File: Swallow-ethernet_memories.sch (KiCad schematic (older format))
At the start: 19 parts, among them P10 A0_Sel, P6 I2C, U10 DRAM-2MX16X4, U8 INA219, U9 S25FL064K

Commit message: Created pinout for SDRAM + ethernet I/O board. Pushed pinout to schematic.
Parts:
- removed C5: 220nF, SM0603, symbol C
- removed P10: A0_Sel, symbol CONN_3
- removed P6: I2C, PIN_ARRAY_4x1, symbol CONN_4
- removed R13, R15: 10R, SM0402, symbol R
- removed R14: 0R1, SM0805, symbol R
- removed R16, R17: 3k3, SM0402, symbol R
- removed U8: INA219, SOT23-8, symbol INA219
- removed W13: A11, TestPad-1mm, symbol TESTPOINT
- removed W14: A12, TestPad-1mm, symbol TESTPOINT
- removed W19: P1G, symbol TESTPOINT
- removed W20: P1F, symbol TESTPOINT
- removed W21: P1K, symbol TESTPOINT
- added P?: Ethernet_Slice, symbol CONN_PCIE-36
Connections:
- net labels added: A1, A2, A3, A4, A5, A6, A7, A8, A9, RESET_N, XLC0i, XLC0o, XLC1i, XLC1o, XLC2i, XLC2o, XLC3i, XLC3o, XLC4i, XLC4o
- net labels removed: P1F, P1G, P1K, SCK, SDA, XLB0i, XLB0o, XLB1i, XLB1o, XLB2i, XLB2o, XLB3i, XLB3o, XLB4i, XLB4o
- wire segments 228 -> 214
- no-connect marks 0 -> 14
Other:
- note added: "B17 is unused INT_N\nB18 in unused RXER"
- note removed: "A12 or D_CLK_EN"
- note removed: "C+D : DRAM Data x16"
- note removed: "DRAM : CLK, CLKEN\nI2C : Clk, Data0, Data1?"
- note removed: "DRAM Address A"
- note removed: "DRAM Current Sensor"
- note removed: "DRAM\nDecoupling"
- note removed: "I2C"
- moved on the sheet: C6, C7

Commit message: Completed schematic.
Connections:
- net labels removed: P32A0
- wire segments 214 -> 209
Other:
- note removed: "Swapped RAS & CAS for library compatibility"
- note removed: "These two pins can be re-used for DRAM clock generation if SPI_SS is set to high(disabled).\n\nOr can they? Since their types are declared "on stdcore[]""
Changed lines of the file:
@@
-EESchema Schematic File Version 2  date 30/09/2012 20:10:30
+EESchema Schematic File Version 2  date 30/09/2012 22:11:50
 LIBS:power
 LIBS:device
@@
 	6300 2400 7250 2400
 Wire Wire Line
-	6300 700  6650 700
-Wire Wire Line
-	6650 700  6650 600
-Wire Wire Line
-	6650 600  9100 600
-Wire Wire Line
 	6300 900  6800 900
 Wire Wire Line
@@
 Wire Wire Line
 	9250 1400 8450 1400
-Wire Wire Line
-	9400 700  9100 700
-Wire Wire Line
-	9100 700  9100 600
 Wire Wire Line
 	10650 2950 10600 2950
@@
 F67 "XLC1i" I L 4450 850 60
 F68 "XLC0i" I L 4450 750 60
+F69 "XLC0o" O L 4450 1650 60
+F70 "XLC1o" O L 4450 1550 60
+F71 "XLC2o" O L 4450 1450 60
+F72 "XLC3o" O L 4450 1350 60
+F73 "XLC4o" O L 4450 1250 60
 $EndSheet
 $Comp
@@
 Text Label 6400 1750 0    60   ~ 0
 P4B0
-Text Label 7750 600  0    60   ~ 0
-P32A0
 Text Label 7350 5000 0    60   ~ 0
 P4B0
@@
 Text Label 7150 1800 0    60   ~ 0
 A12
-Text Notes 6450 6550 0    60   ~ 0
-These two pins can be re-used for DRAM clock generation if SPI_SS is set to high(disabled).\n\nOr can they? Since their types are declared "on stdcore[]"
-Text Notes 6900 4750 0    60   ~ 0
-Swapped RAS & CAS for library compatibility
 Text Label 6350 4600 0    60   ~ 0
 CS_N

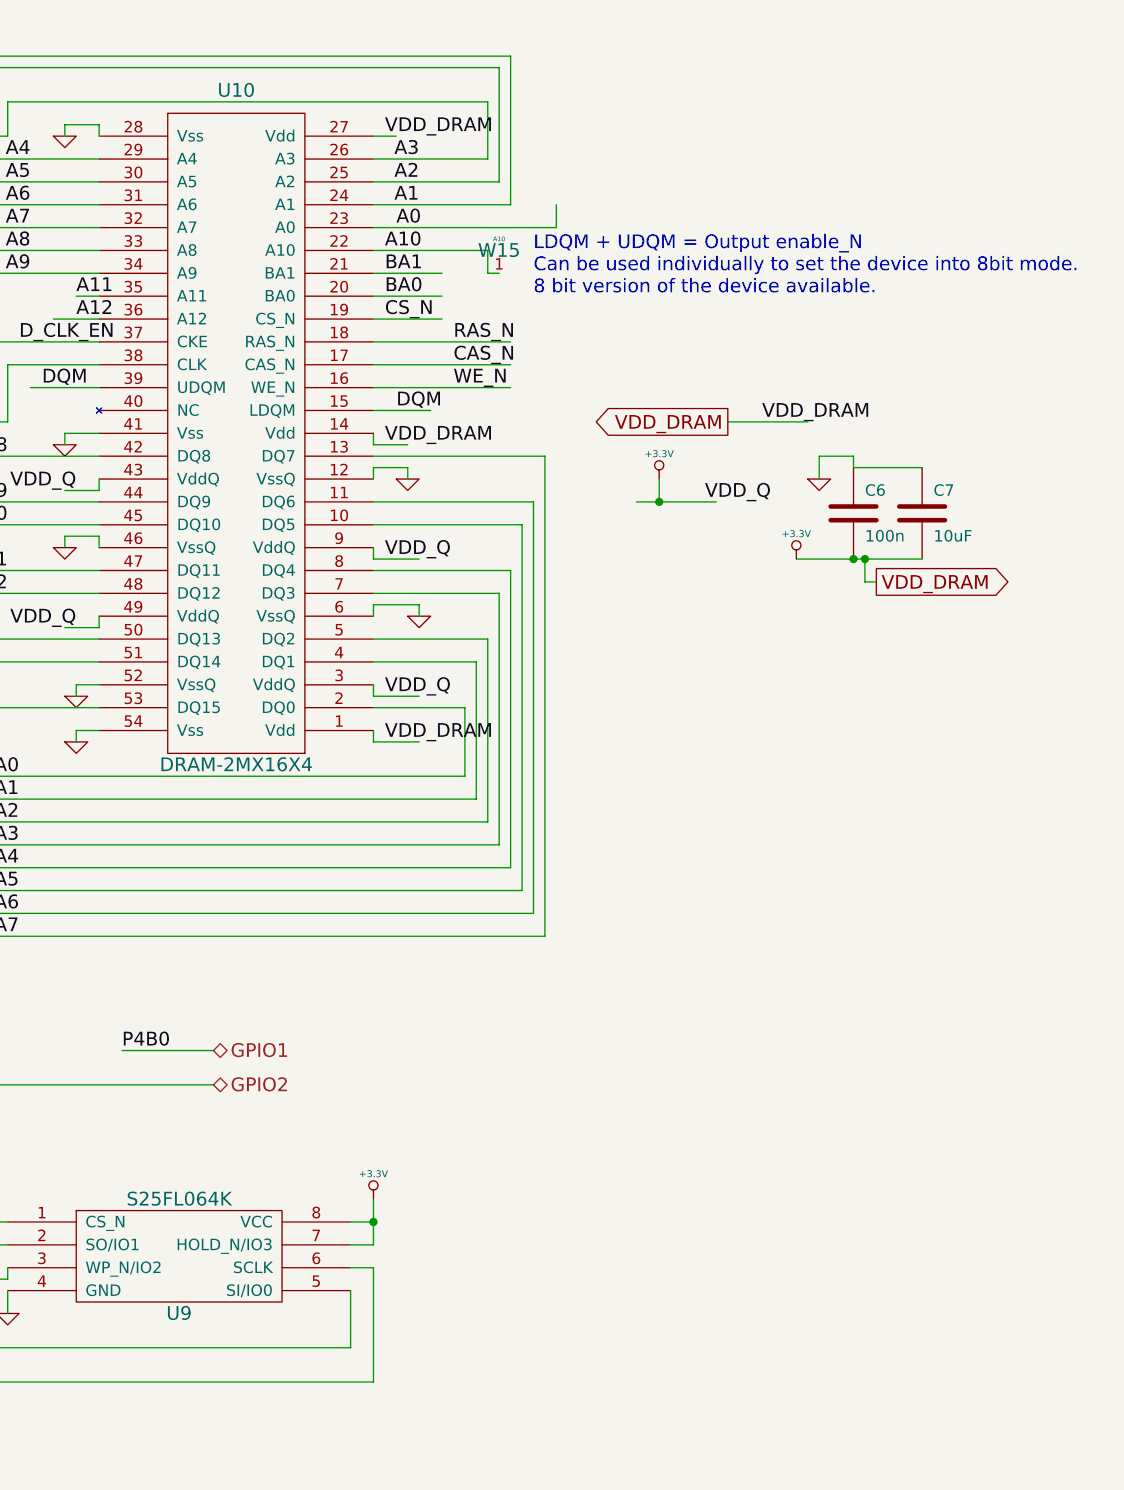
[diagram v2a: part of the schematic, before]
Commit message: Re-annotated schematic and deleted redundant components from PCB design.
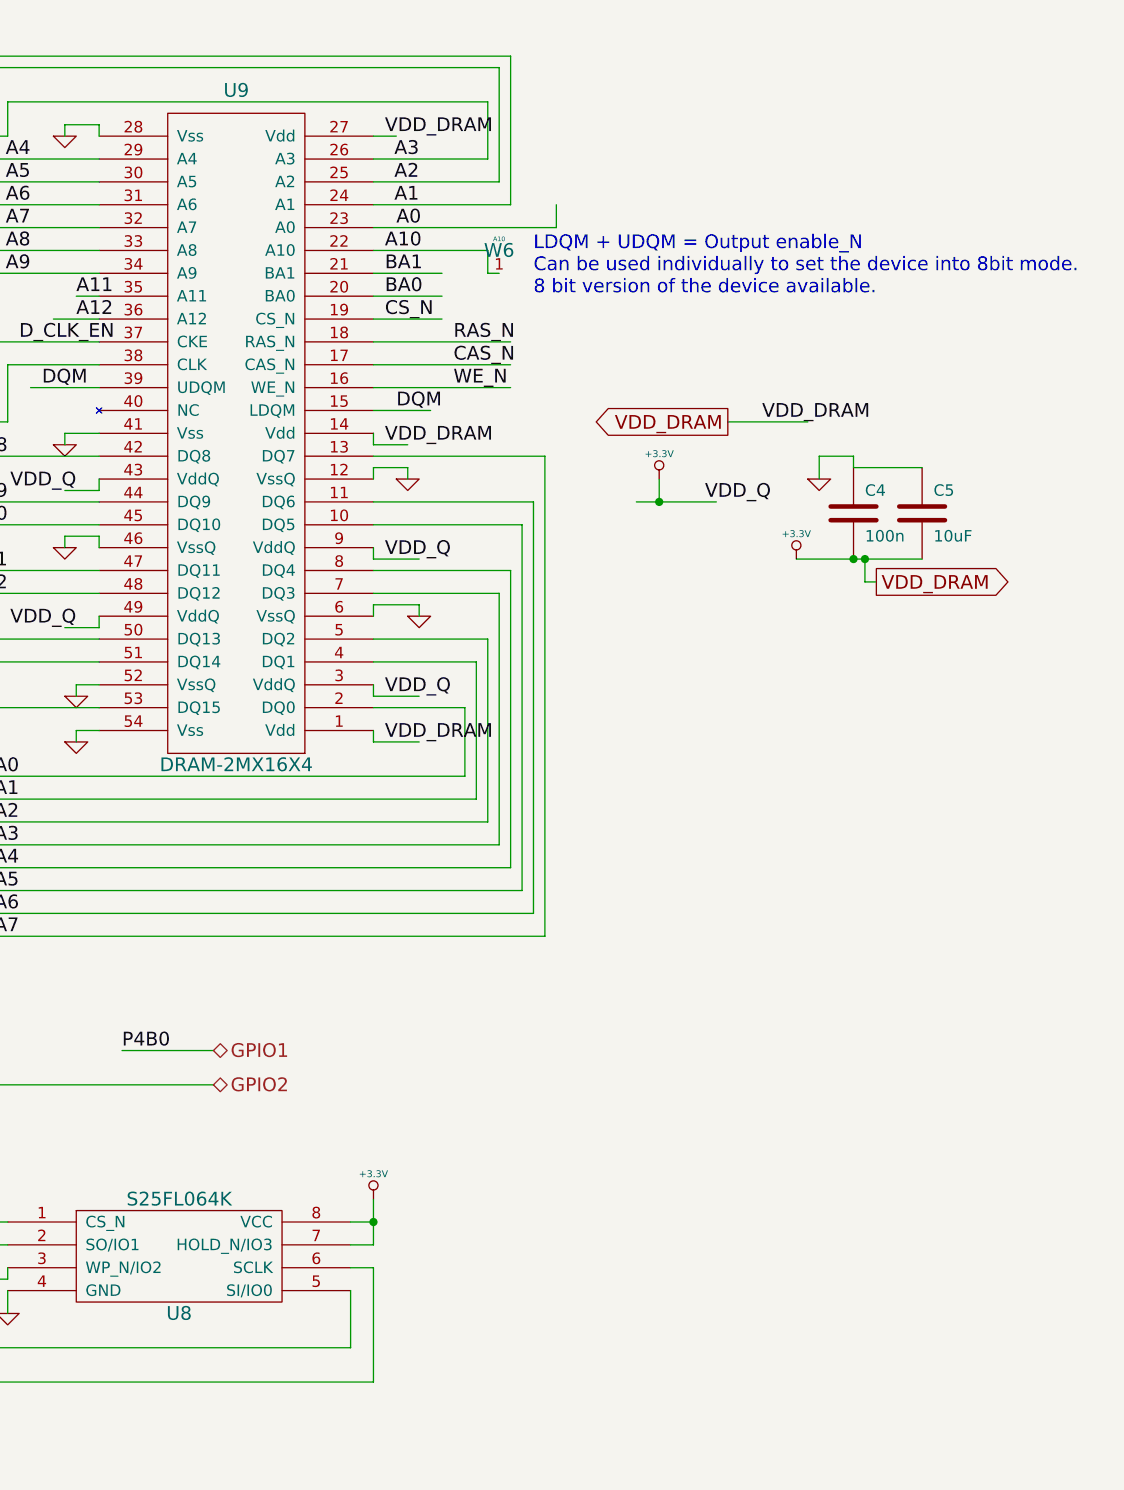
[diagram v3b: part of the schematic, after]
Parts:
- gave numbers to parts that had none: 1
- renumbered C6 to C4, C7 to C5, U9 to U8, U10 to U9, W15 to W6
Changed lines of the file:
@@
-EESchema Schematic File Version 2  date 30/09/2012 22:11:50
+EESchema Schematic File Version 2  date 30/09/2012 22:23:08
 LIBS:power
 LIBS:device
@@
 B17 is unused INT_N\nB18 in unused RXER
 $Comp
-L +3.3V #PWR?
+L +3.3V #PWR031
 U 1 1 506889FB
 P 2200 3800
-F 0 "#PWR?" H 2200 3760 30  0001 C CNN
+F 0 "#PWR031" H 2200 3760 30  0001 C CNN
 F 1 "+3.3V" H 2200 3910 30  0000 C CNN
 	1    2200 3800
@@
 NoConn ~ 2900 5200
 $Comp
-L GND #PWR?
+L GND #PWR032
 U 1 1 506889D0
 P 2800 5300
-F 0 "#PWR?" H 2800 5300 30  0001 C CNN
+F 0 "#PWR032" H 2800 5300 30  0001 C CNN
 F 1 "GND" H 2800 5230 30  0001 C CNN
 	1    2800 5300
@@
 $EndComp
 $Comp
-L GND #PWR?
+L GND #PWR033
 U 1 1 506889CC
 P 3800 5300
-F 0 "#PWR?" H 3800 5300 30  0001 C CNN
+F 0 "#PWR033" H 3800 5300 30  0001 C CNN
 F 1 "GND" H 3800 5230 30  0001 C CNN
 	1    3800 5300
@@
 $EndSheet
 $Comp
-L CONN_PCIE-36 P?
+L CONN_PCIE-36 P5
 U 1 1 50688658
 P 3300 4350
-F 0 "P?" H 3300 5400 60  0000 C CNN
+F 0 "P5" H 3300 5400 60  0000 C CNN
 F 1 "Ethernet_Slice" V 3300 4350 50  0000 C CNN
 	1    3300 4350
@@
 A9
 $Comp
-L +3.3V #PWR?
+L +3.3V #PWR034
 U 1 1 506882AB
 P 10300 2850
-F 0 "#PWR?" H 10300 2810 30  0001 C CNN
+F 0 "#PWR034" H 10300 2810 30  0001 C CNN
 F 1 "+3.3V" H 10300 2960 30  0000 C CNN
 	1    10300 2850
@@
 $EndComp
 $Comp
-L C C6
+L C C4
 U 1 1 4F5B61BC
 P 10550 2650
-F 0 "C6" H 10600 2750 50  0000 L CNN
+F 0 "C4" H 10600 2750 50  0000 L CNN
 F 1 "100n" H 10600 2550 50  0000 L CNN
 F 2 "SM0603" H 10600 2650 50  0001 C CNN
@@
 $EndComp
 $Comp
-L C C7
+L C C5
 U 1 1 4F5B90F2
 P 10850 2650
-F 0 "C7" H 10900 2750 50  0000 L CNN
+F 0 "C5" H 10900 2750 50  0000 L CNN
 F 1 "10uF" H 10900 2550 50  0000 L CNN
 F 2 "SM0805" H 10900 2650 50  0001 C CNN
@@
 $EndComp
 $Comp
-L GND #PWR055
+L GND #PWR035
 U 1 1 4F5B70D6
 P 10400 2500
-F 0 "#PWR055" H 10400 2500 30  0001 C CNN
+F 0 "#PWR035" H 10400 2500 30  0001 C CNN
 F 1 "GND" H 10400 2430 30  0001 C CNN
 	1    10400 2500
@@
 DRAM_CLK
 $Comp
-L TESTPOINT W15
+L TESTPOINT W6
 U 1 1 4F622603
 P 9000 1450
-F 0 "W15" H 9000 1400 60  0000 C CNN
+F 0 "W6" H 9000 1400 60  0000 C CNN
 F 1 "A10" H 9000 1450 20  0000 C CNN
 F 2 "TestPad-1mm" H 9000 1550 20  0001 C CNN
@@
 $EndComp
 $Comp
-L DRAM-4MX16X4 U10
+L DRAM-4MX16X4 U9
 U 1 1 4F5A335A
 P 7700 2200
-F 0 "U10" H 7550 800 60  0000 C CNN
+F 0 "U9" H 7550 800 60  0000 C CNN
 F 1 "DRAM-2MX16X4" H 7550 3750 60  0000 C CNN
 F 2 "TSSOP-54" H 7550 3850 60  0001 C CNN
@@
 D_CLK_EN
 $Comp
-L +3.3V #PWR051
+L +3.3V #PWR036
 U 1 1 4F5D0367
 P 9700 2500
-F 0 "#PWR051" H 9700 2460 30  0001 C CNN
+F 0 "#PWR036" H 9700 2460 30  0001 C CNN
 F 1 "+3.3V" H 9700 2610 30  0000 C CNN
 	1    9700 2500
@@
 VDD_Q
 $Comp
-L GND #PWR054
+L GND #PWR037
 U 1 1 4F5BE236
 P 7150 3450
-F 0 "#PWR054" H 7150 3450 30  0001 C CNN
+F 0 "#PWR037" H 7150 3450 30  0001 C CNN
 F 1 "GND" H 7150 3380 30  0001 C CNN
 	1    7150 3450
@@
 GPIO1
 $Comp
-L GND #PWR059
+L GND #PWR038
 U 1 1 4F5B6D20
 P 6850 6150
-F 0 "#PWR059" H 6850 6150 30  0001 C CNN
+F 0 "#PWR038" H 6850 6150 30  0001 C CNN
 F 1 "GND" H 6850 6080 30  0001 C CNN
 	1    6850 6150
@@
 $EndComp
 $Comp
-L +3.3V #PWR060
+L +3.3V #PWR039
 U 1 1 4F5B6D1D
 P 6650 6000
-F 0 "#PWR060" H 6650 5960 30  0001 C CNN
+F 0 "#PWR039" H 6650 5960 30  0001 C CNN
 F 1 "+3.3V" H 6650 6110 30  0000 C CNN
 	1    6650 6000
@@
 $EndComp
 $Comp
-L +3.3V #PWR061
+L +3.3V #PWR040
 U 1 1 4F5B6D0E
 P 8450 5650
-F 0 "#PWR061" H 8450 5610 30  0001 C CNN
+F 0 "#PWR040" H 8450 5610 30  0001 C CNN
 F 1 "+3.3V" H 8450 5760 30  0000 C CNN
 	1    8450 5650
@@
 BA1
 $Comp
-L GND #PWR065
+L GND #PWR041
 U 1 1 4F5B65E9
 P 7100 2350
-F 0 "#PWR065" H 7100 2350 30  0001 C CNN
+F 0 "#PWR041" H 7100 2350 30  0001 C CNN
 F 1 "GND" H 7100 2280 30  0001 C CNN
 	1    7100 2350
@@
 LDQM + UDQM = Output enable_N\nCan be used individually to set the device into 8bit mode.\n8 bit version of the device available.
 $Comp
-L GND #PWR066
+L GND #PWR042
 U 1 1 4F5B60D8
 P 7100 1000
-F 0 "#PWR066" H 7100 1000 30  0001 C CNN
+F 0 "#PWR042" H 7100 1000 30  0001 C CNN
 F 1 "GND" H 7100 930 30  0001 C CNN
 	1    7100 1000
@@
 $EndComp
 $Comp
-L GND #PWR067
+L GND #PWR043
 U 1 1 4F5B60D1
 P 8600 2500
-F 0 "#PWR067" H 8600 2500 30  0001 C CNN
+F 0 "#PWR043" H 8600 2500 30  0001 C CNN
 F 1 "GND" H 8600 2430 30  0001 C CNN
 	1    8600 2500
@@
 $EndComp
 $Comp
-L GND #PWR068
+L GND #PWR044
 U 1 1 4F5B60CC
 P 7100 2800
-F 0 "#PWR068" H 7100 2800 30  0001 C CNN
+F 0 "#PWR044" H 7100 2800 30  0001 C CNN
 F 1 "GND" H 7100 2730 30  0001 C CNN
 	1    7100 2800
@@
 $EndComp
 $Comp
-L GND #PWR069
+L GND #PWR045
 U 1 1 4F5B60C1
 P 8650 3100
-F 0 "#PWR069" H 8650 3100 30  0001 C CNN
+F 0 "#PWR045" H 8650 3100 30  0001 C CNN
 F 1 "GND" H 8650 3030 30  0001 C CNN
 	1    8650 3100
@@
 $EndComp
 $Comp
-L GND #PWR070
+L GND #PWR046
 U 1 1 4F5B5F9C
 P 7150 3650
-F 0 "#PWR070" H 7150 3650 30  0001 C CNN
+F 0 "#PWR046" H 7150 3650 30  0001 C CNN
 F 1 "GND" H 7150 3580 30  0001 C CNN
 	1    7150 3650
@@
 $EndComp
 $Comp
-L S25FL064K U9
+L S25FL064K U8
 U 1 1 4F5B5AA3
 P 7650 5900
-F 0 "U9" H 7600 5650 60  0000 C CNN
+F 0 "U8" H 7600 5650 60  0000 C CNN
 F 1 "S25FL064K" H 7600 6150 60  0000 C CNN
 F 2 "SO8NL" H 7600 6250 60  0001 C CNN
